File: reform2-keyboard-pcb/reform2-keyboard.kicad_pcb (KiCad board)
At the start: 2 copper layers, 275.9 x 117.8 mm, 291 parts, among them J1 USB, J2 UART, J3 AUX, J4 USB_C_Receptacle_USB2.0, SW1 Choc, SW10 Choc, SW11 Choc, SW12 Choc, SW13 Choc, SW14 Choc, SW15 Choc, SW16 Choc, SW17 Choc, SW18 Choc, SW19 Choc, SW2 Choc, SW20 Choc, SW21 Choc, SW22 Choc, SW23 Choc, SW24 Choc, SW25 Choc, SW26 Choc, SW27 Choc, SW28 Choc, SW29 Choc, SW3 Choc, SW30 Choc, SW31 Choc, SW32 Choc, SW33 Choc, SW34 Choc, SW35 Choc, SW36 Choc, SW37 Choc, SW38 Choc, SW39 Choc, SW4 Choc, SW40 Choc, SW41 Choc, SW42 Choc, SW43 Choc, SW44 Choc, SW45 Choc, SW46 Choc, SW47 Choc, SW48 Choc, SW49 Choc, SW5 Choc, SW50 Choc, SW51 Choc, SW52 Choc, SW53 Choc, SW54 Choc, SW55 Choc, SW56 Choc, SW57 Choc, SW58 Choc, SW59 Choc, SW6 Choc, SW60 Choc, SW61 Choc, SW62 Choc, SW63 Choc, SW64 Choc, SW65 Choc, SW66 Choc, SW67 Choc, SW68 Choc, SW69 Choc, SW7 Choc, SW70 Choc, SW71 Choc, SW72 Choc, SW73 Choc, SW74 Choc, SW75 Choc, SW76 Choc, SW77 Choc, SW78 Choc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

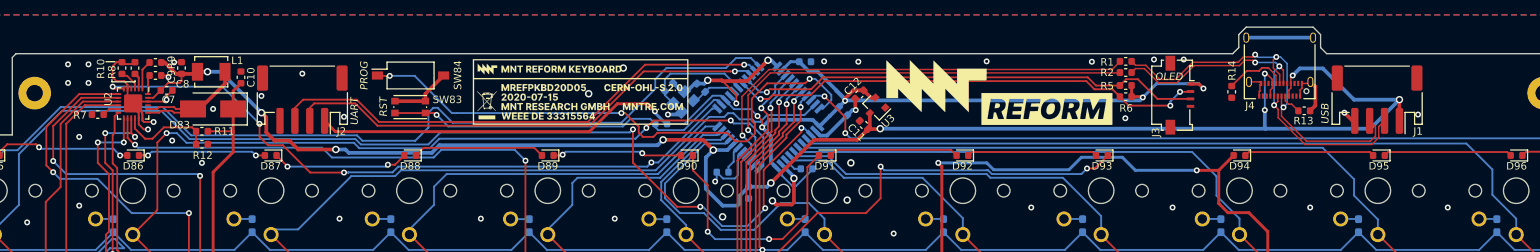
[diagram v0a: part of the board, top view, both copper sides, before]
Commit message: reform2: update PCBs incl. badges to production revs, add keyboard lettering, misc docs
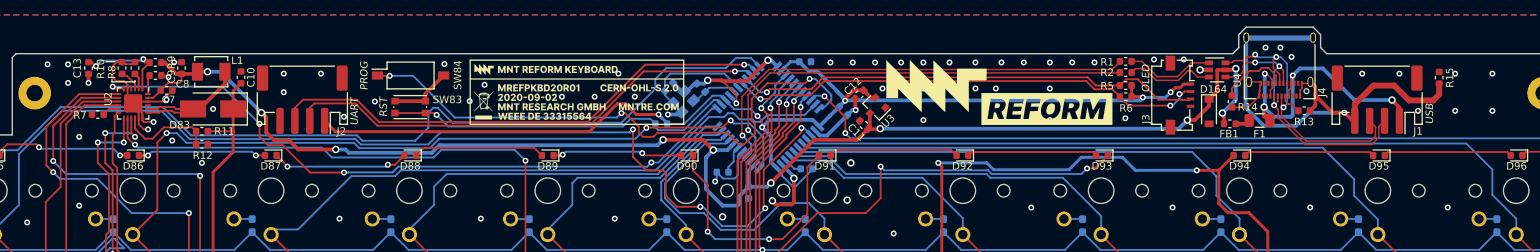
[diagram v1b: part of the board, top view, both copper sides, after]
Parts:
- removed G***: LOGO, reform2-keyboard:mntreform-keyboard-badge
- added C13: 1uF, Capacitor_SMD:C_0603_1608Metric, F.Cu at (48.8, 21.8)
- added D164: BZT52-B5V6J, Diode_SMD:D_SOD-123, F.Cu at (199.4, 27.6)
- added F1: 0ZCJ0075AF2E, Resistor_SMD:R_1206_3216Metric, F.Cu at (206.2, 28.8)
- added FB1: BLM18PG221SH1D, Inductor_SMD:L_0603_1608Metric, F.Cu at (202.2, 29.2)
- added GFX3: MNT, reform2-keyboard:mntreform-keyboard-badge, F.Cu at (114.4, 25.0)
- added R15: 0, Resistor_SMD:R_0603_1608Metric, F.Cu at (230.3, 23.1)
- added U4: USBLC6-2SC6, Package_TO_SOT_SMD:SOT-23-6, F.Cu at (200.5, 22.0)
- R9: value 0 -> 4.7k
- moved R14 1.30 mm to (202.5, 26.2)
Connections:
- J1 pad 1: +5V -> Net-(F1-Pad1)
- J1 pad 2: D- -> HD-
- J1 pad 3: D+ -> HD+
- J1 pad 4: GND -> Net-(J1-Pad4)
- J4 pad A1: GND -> Net-(J1-Pad4)
- J4 pad A12: GND -> Net-(J1-Pad4)
- J4 pad A4: +5V -> Net-(F1-Pad1)
- J4 pad A6: D+ -> HD+
- J4 pad A7: D- -> HD-
- J4 pad A9: +5V -> Net-(F1-Pad1)
- J4 pad B1: GND -> Net-(J1-Pad4)
- J4 pad B12: GND -> Net-(J1-Pad4)
- J4 pad B4: +5V -> Net-(F1-Pad1)
- J4 pad B6: D+ -> HD+
- J4 pad B7: D- -> HD-
- J4 pad B9: +5V -> Net-(F1-Pad1)
- J4 pad S1: GND -> Net-(J1-Pad4)
- R13 pad 1: GND -> Net-(J1-Pad4)
- R14 pad 2: GND -> Net-(J1-Pad4)
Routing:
- net Net-(J1-Pad4): track 0.00 -> 73.0 mm, vias 0 -> 1
- net +5V: track 236.9 -> 193.7 mm, vias 11 -> 10
- net Net-(F1-Pad1): track 0.00 -> 42.3 mm, vias 0 -> 4
- net D+: track 53.6 -> 12.0 mm, vias 3 -> 0
- net D-: track 51.8 -> 12.1 mm, vias 3 -> 0
- net HD+: track 0.00 -> 39.1 mm, vias 0 -> 3
- net HD-: track 0.00 -> 38.1 mm, vias 0 -> 3
- net GND: track 107.5 -> 88.1 mm, vias 87 -> 119
- net Net-(C13-Pad1): track 3.91 -> 12.8 mm, vias 0 -> 2
- net +3V3: track 165.6 -> 161.5 mm
- net Net-(F1-Pad2): track 0.00 -> 1.92 mm
- net COL2: track 245.2 -> 246.5 mm
- net Net-(J4-PadB5): track 8.45 -> 9.52 mm
- net PROG: track 76.1 -> 76.9 mm

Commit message: keyboard: add pcb version that has almost all components on the front side, with parts from lcsc
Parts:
- added J5: AVR-ISP-6, Connector_PinHeader_2.54mm:PinHeader_2x03_P2.54mm_Vertical, F.Cu at (98.8, 22.2)
- added R16: 10k, Resistor_SMD:R_0603_1608Metric, F.Cu at (119.8, 24.2)
- added R17: 22, Resistor_SMD:R_0603_1608Metric, F.Cu at (104.8, 22.2)
- added R18: 22, Resistor_SMD:R_0603_1608Metric, F.Cu at (104.8, 24.2)
- added R19: 22, Resistor_SMD:R_0603_1608Metric, F.Cu at (104.8, 26.2)
- C1, C2, C3, C4, C5, C6, D1, D10, D11, D12, D13, D14, D15, D16, D17, D18, D19, D2, D20, D21, D22, D23, D24, D25, D26, D27, D28, D29, D3, D30, D31, D32, D33, D34, D35, D36, D37, D38, D39, D4, D40, D41, D42, D43, D44, D45, D46, D47, D48, D49, D5, D50, D51, D52, D53, D54, D55, D56, D57, D58, D59, D6, D60, D61, D62, D63, D64, D65, D66, D67, D68, D69, D7, D70, D71, D72, D73, D74, D75, D76, D77, D78, D79, D8, D80, D81, D82, D9, R3, R4, Y1: moved to F.Cu
- GFX3: footprint reform2-keyboard:mntreform-keyboard-badge -> footprints:mnt-reform-keyboard-r2-badge; moved to B.Cu
- J4: footprint Connector_USB:USB_C_Receptacle_Amphenol_12401610E4-2A -> Connector_USB:USB_C_Receptacle_HRO_TYPE-C-31-M-12
- moved D43 12.2 mm to (157.0, 40.2)
- moved R4 11.7 mm to (157.0, 35.0), turned to 90 degrees
- moved D42 11.1 mm to (161.8, 129.9)
- moved C3 8.62 mm to (138.2, 43.2), turned to 90 degrees
- moved D1 7.97 mm to (8.75, 38.0)
- moved D49 6.78 mm to (157.0, 44.0)
- moved D10 6.25 mm to (27.4, 95.7)
- moved D11 6.25 mm to (36.3, 113.2)
- moved D12 6.25 mm to (41.0, 129.9)
- moved D13 6.25 mm to (45.9, 42.9)
- moved D14 6.25 mm to (46.0, 60.5)
- moved D15 6.25 mm to (55.0, 78.1)
- moved D16 6.25 mm to (46.0, 95.7)
- moved D17 6.25 mm to (54.9, 113.3)
- moved D18 6.25 mm to (69.0, 129.9)
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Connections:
- J3 pad 1: +3V3 -> GND
- J3 pad 2: DISP_SCL -> DISP_SDA
- J3 pad 3: DISP_SDA -> DISP_SCL
- J3 pad 4: GND -> +3V3
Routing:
- net COL7: track 159.9 -> 193.9 mm, vias 4 -> 7
- net COL5: track 170.3 -> 197.5 mm, vias 0 -> 3
- net COL6: track 163.0 -> 188.9 mm, vias 2 -> 5
- net ROW6: track 382.3 -> 405.9 mm, vias 2 -> 14
- net +3V3: track 161.5 -> 184.1 mm, vias 6 -> 8
- net Net-(J1-Pad4): track 73.0 -> 53.1 mm, vias 1 -> 0
- net Net-(D43-Pad2): track 2.41 -> 17.6 mm, vias 0 -> 1
- net Net-(R4-Pad1): track 2.43 -> 17.3 mm, vias 0 -> 1
- net ROW4: track 351.5 -> 364.7 mm, vias 2 -> 15
- net ROW3: track 334.1 -> 347.0 mm, vias 2 -> 16
- net Net-(C10-Pad1): track 530.4 -> 543.1 mm
- net ROW1: track 295.9 -> 308.2 mm, vias 2 -> 15
- net ROW5: track 374.2 -> 385.5 mm, vias 2 -> 15
- net Net-(F1-Pad1): track 42.3 -> 31.1 mm, vias 4 -> 3
- net ROW2: track 313.9 -> 325.0 mm, vias 2 -> 15
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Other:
- rule pad_to_mask_clearance: 0.2 -> 0
- board text added: "ICSP"
- board text added: "PRG"
- board text removed: "PROG"

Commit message: keyboard: add WIP R-2D version, atmega RC notes
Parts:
- added TP1: TP, TestPoint:TestPoint_Pad_1.0x1.0mm, B.Cu at (97.5, 102.2)
- added TP10: TP, TestPoint:TestPoint_Pad_1.0x1.0mm, B.Cu at (206.5, 35.2)
- added TP11: TP, TestPoint:TestPoint_Pad_1.0x1.0mm, B.Cu at (135.2, 51.0)
- added TP12: TP, TestPoint:TestPoint_Pad_1.0x1.0mm, B.Cu at (67.8, 68.8)
- added TP13: TP, TestPoint:TestPoint_Pad_1.0x1.0mm, B.Cu at (253.5, 68.8)
- added TP14: TP, TestPoint:TestPoint_Pad_1.0x1.0mm, B.Cu at (170.5, 86.2)
- added TP15: TP, TestPoint:TestPoint_Pad_1.0x1.0mm, B.Cu at (104.8, 103.8)
- added TP16: TP, TestPoint:TestPoint_Pad_1.0x1.0mm, B.Cu at (25.8, 121.5)
- added TP17: TP, TestPoint:TestPoint_Pad_1.0x1.0mm, B.Cu at (44.2, 32.8)
- added TP18: TP, TestPoint:TestPoint_Pad_1.0x1.0mm, B.Cu at (225.2, 35.2)
- added TP19: TP, TestPoint:TestPoint_Pad_1.0x1.0mm, B.Cu at (151.8, 51.0)
- added TP20: TP, TestPoint:TestPoint_Pad_1.0x1.0mm, B.Cu at (86.2, 68.8)
- added TP21: TP, TestPoint:TestPoint_Pad_1.0x1.0mm, B.Cu at (18.8, 82.5)
- added TP22: TP, TestPoint:TestPoint_Pad_1.0x1.0mm, B.Cu at (189.8, 86.2)
- added TP23: TP, TestPoint:TestPoint_Pad_1.0x1.0mm, B.Cu at (123.5, 103.8)
- added TP24: TP, TestPoint:TestPoint_Pad_1.0x1.0mm, B.Cu at (53.5, 121.5)
- added TP25: TP, TestPoint:TestPoint_Pad_1.0x1.0mm, B.Cu at (58.5, 33.5)
- added TP26: TP, TestPoint:TestPoint_Pad_1.0x1.0mm, B.Cu at (243.8, 35.2)
- added TP27: TP, TestPoint:TestPoint_Pad_1.0x1.0mm, B.Cu at (170.0, 51.0)
- added TP28: TP, TestPoint:TestPoint_Pad_1.0x1.0mm, B.Cu at (104.8, 68.8)
- added TP29: TP, TestPoint:TestPoint_Pad_1.0x1.0mm, B.Cu at (21.2, 86.2)
- added TP30: TP, TestPoint:TestPoint_Pad_1.0x1.0mm, B.Cu at (207.2, 86.2)
- added TP31: TP, TestPoint:TestPoint_Pad_1.0x1.0mm, B.Cu at (141.8, 103.8)
- added TP32: TP, TestPoint:TestPoint_Pad_1.0x1.0mm, B.Cu at (125.0, 121.5)
- added TP33: TP, TestPoint:TestPoint_Pad_1.0x1.0mm, B.Cu at (77.2, 35.0)
- added TP34: TP, TestPoint:TestPoint_Pad_1.0x1.0mm, B.Cu at (18.5, 48.8)
- added TP35: TP, TestPoint:TestPoint_Pad_1.0x1.0mm, B.Cu at (188.5, 51.0)
- added TP36: TP, TestPoint:TestPoint_Pad_1.0x1.0mm, B.Cu at (123.2, 68.8)
- added TP37: TP, TestPoint:TestPoint_Pad_1.0x1.0mm, B.Cu at (39.8, 86.2)
- added TP38: TP, TestPoint:TestPoint_Pad_1.0x1.0mm, B.Cu at (226.0, 86.2)
- added TP39: TP, TestPoint:TestPoint_Pad_1.0x1.0mm, B.Cu at (160.5, 103.8)
- added TP40: TP, TestPoint:TestPoint_Pad_1.0x1.0mm, B.Cu at (132.5, 121.5)
- added TP41: TP, TestPoint:TestPoint_Pad_1.0x1.0mm, B.Cu at (98.5, 33.8)
- added TP42: TP, TestPoint:TestPoint_Pad_1.0x1.0mm, B.Cu at (21.2, 51.0)
- added TP43: TP, TestPoint:TestPoint_Pad_1.0x1.0mm, B.Cu at (207.2, 51.0)
- added TP44: TP, TestPoint:TestPoint_Pad_1.0x1.0mm, B.Cu at (141.8, 68.8)
- added TP45: TP, TestPoint:TestPoint_Pad_1.0x1.0mm, B.Cu at (58.5, 86.2)
- added TP46: TP, TestPoint:TestPoint_Pad_1.0x1.0mm, B.Cu at (244.5, 86.2)
- added TP47: TP, TestPoint:TestPoint_Pad_1.0x1.0mm, B.Cu at (179.2, 103.8)
- added TP48: TP, TestPoint:TestPoint_Pad_1.0x1.0mm, B.Cu at (151.2, 121.5)
- added TP49: TP, TestPoint:TestPoint_Pad_1.0x1.0mm, B.Cu at (114.2, 33.5)
- added TP50: TP, TestPoint:TestPoint_Pad_1.0x1.0mm, B.Cu at (40.0, 51.0)
- added TP51: TP, TestPoint:TestPoint_Pad_1.0x1.0mm, B.Cu at (225.8, 51.0)
- added TP52: TP, TestPoint:TestPoint_Pad_1.0x1.0mm, B.Cu at (160.5, 68.8)
- added TP53: TP, TestPoint:TestPoint_Pad_1.0x1.0mm, B.Cu at (77.0, 86.2)
- added TP54: TP, TestPoint:TestPoint_Pad_1.0x1.0mm, B.Cu at (266.5, 88.0)
- added TP55: TP, TestPoint:TestPoint_Pad_1.0x1.0mm, B.Cu at (197.8, 103.8)
- added TP56: TP, TestPoint:TestPoint_Pad_1.0x1.0mm, B.Cu at (197.8, 121.5)
- added TP57: TP, TestPoint:TestPoint_Pad_1.0x1.0mm, B.Cu at (131.8, 44.0)
- added TP58: TP, TestPoint:TestPoint_Pad_1.0x1.0mm, B.Cu at (58.8, 51.0)
- added TP59: TP, TestPoint:TestPoint_Pad_1.0x1.0mm, B.Cu at (244.5, 51.0)
- added TP60: TP, TestPoint:TestPoint_Pad_1.0x1.0mm, B.Cu at (179.0, 68.8)
- added TP61: TP, TestPoint:TestPoint_Pad_1.0x1.0mm, B.Cu at (95.8, 86.2)
- added TP62: TP, TestPoint:TestPoint_Pad_1.0x1.0mm, B.Cu at (25.8, 103.8)
- added TP63: TP, TestPoint:TestPoint_Pad_1.0x1.0mm, B.Cu at (216.5, 103.8)
- added TP64: TP, TestPoint:TestPoint_Pad_1.0x1.0mm, B.Cu at (216.2, 121.5)
- added TP65: TP, TestPoint:TestPoint_Pad_1.0x1.0mm, B.Cu at (159.8, 34.0)
- added TP66: TP, TestPoint:TestPoint_Pad_1.0x1.0mm, B.Cu at (77.5, 51.0)
- added TP67: TP, TestPoint:TestPoint_Pad_1.0x1.0mm, B.Cu at (23.8, 65.0)
- added TP68: TP, TestPoint:TestPoint_Pad_1.0x1.0mm, B.Cu at (197.8, 68.8)
- added TP69: TP, TestPoint:TestPoint_Pad_1.0x1.0mm, B.Cu at (114.2, 86.2)
- added TP70: TP, TestPoint:TestPoint_Pad_1.0x1.0mm, B.Cu at (49.0, 103.8)
- added TP71: TP, TestPoint:TestPoint_Pad_1.0x1.0mm, B.Cu at (235.0, 103.8)
- added TP72: TP, TestPoint:TestPoint_Pad_1.0x1.0mm, B.Cu at (235.0, 121.5)
- added TP73: TP, TestPoint:TestPoint_Pad_1.0x1.0mm, B.Cu at (177.8, 34.8)
- added TP74: TP, TestPoint:TestPoint_Pad_1.0x1.0mm, B.Cu at (96.0, 51.0)
- added TP75: TP, TestPoint:TestPoint_Pad_1.0x1.0mm, B.Cu at (25.8, 68.8)
- added TP76: TP, TestPoint:TestPoint_Pad_1.0x1.0mm, B.Cu at (216.2, 68.8)
- added TP77: TP, TestPoint:TestPoint_Pad_1.0x1.0mm, B.Cu at (133.0, 86.2)
- added TP78: TP, TestPoint:TestPoint_Pad_1.0x1.0mm, B.Cu at (67.5, 103.8)
- added TP79: TP, TestPoint:TestPoint_Pad_1.0x1.0mm, B.Cu at (253.5, 103.8)
- added TP80: TP, TestPoint:TestPoint_Pad_1.0x1.0mm, B.Cu at (253.5, 121.5)
- added TP81: TP, TestPoint:TestPoint_Pad_1.0x1.0mm, B.Cu at (181.2, 35.2)
- added TP82: TP, TestPoint:TestPoint_Pad_1.0x1.0mm, B.Cu at (114.0, 51.0)
- added TP83: TP, TestPoint:TestPoint_Pad_1.0x1.0mm, B.Cu at (48.8, 68.8)
- added TP84: TP, TestPoint:TestPoint_Pad_1.0x1.0mm, B.Cu at (227.5, 70.0)
- added TP85: TP, TestPoint:TestPoint_Pad_1.0x1.0mm, B.Cu at (152.0, 86.2)
- added TP86: TP, TestPoint:TestPoint_Pad_1.0x1.0mm, B.Cu at (86.2, 103.8)
- added TP87: TP, TestPoint:TestPoint_Pad_1.0x1.0mm, B.Cu at (260.2, 101.5)
- added TP88: TP, TestPoint:TestPoint_Pad_1.0x1.0mm, B.Cu at (264.8, 122.8)
- added TP9: TP, TestPoint:TestPoint_Pad_1.0x1.0mm, B.Cu at (32.8, 34.2)
- D1, D10, D11, D12, D13, D14, D15, D16, D17, D18, D19, D2, D20, D21, D22, D23, D24, D25, D26, D27, D28, D29, D3, D30, D31, D32, D33, D34, D35, D36, D37, D38, D39, D4, D40, D41, D42, D43, D44, D45, D46, D47, D48, D49, D5, D50, D51, D52, D53, D54, D55, D56, D57, D58, D59, D6, D60, D61, D62, D63, D64, D65, D66, D67, D68, D69, D7, D70, D71, D72, D73, D74, D75, D76, D77, D78, D79, D8, D80, D81, D82, D9: moved to B.Cu
- moved D143 0.25 mm to (82.2, 103.8)
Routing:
- net ROW6: track 405.9 -> 380.0 mm, vias 14 -> 2
- net Net-(C10-Pad1): track 543.1 -> 536.1 mm, vias 14 -> 12
- net Net-(D143-Pad1): track 126.8 -> 129.9 mm
- net Net-(D103-Pad1): track 76.6 -> 79.6 mm, vias 2 -> 3
- net Net-(D133-Pad1): track 172.7 -> 175.4 mm
- net Net-(D92-Pad1): track 17.6 -> 20.2 mm, vias 0 -> 1
- net Net-(D19-Pad2): track 6.00 -> 3.81 mm, vias 1 -> 0
- net Net-(D43-Pad2): track 17.6 -> 15.4 mm, vias 1 -> 0
- net Net-(D88-Pad1): track 17.8 -> 19.6 mm, vias 0 -> 1
- net Net-(D95-Pad1): track 17.3 -> 18.9 mm, vias 0 -> 1
- net ROW1: track 308.2 -> 306.6 mm, vias 15 -> 2
- net Net-(D96-Pad1): track 21.8 -> 23.4 mm, vias 0 -> 1
- net COL8: track 173.8 -> 172.3 mm
- net Net-(D84-Pad1): track 17.5 -> 19.0 mm, vias 0 -> 1
- net ROW3: track 347.0 -> 345.6 mm, vias 16 -> 2
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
